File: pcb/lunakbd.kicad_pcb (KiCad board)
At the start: 2 copper layers, 134.4 x 112.7 mm, 64 parts, among them J1 TRRS-PJ-320D, J2 Battery_Socket, J3 Conn_Display, SW1 Switch, SW10 Switch, SW11 Switch, SW12 Switch, SW13 Switch, SW14 Switch, SW15 Switch, SW16 Switch, SW17 Switch, SW18 Switch, SW19 Switch, SW2 Switch, SW20 Switch, SW21 Switch, SW22 Switch, SW23 Switch, SW24 Switch, SW25 Switch, SW26 Switch, SW27 Switch, SW28 Switch, SW29 RotaryEncoder_SW, SW3 Switch, SW30 Reset_Button, SW31 Battery_Switch, SW4 Switch, SW5 Switch, SW6 Switch, SW7 Switch, SW8 Switch, SW9 Switch, U1 ProMicro

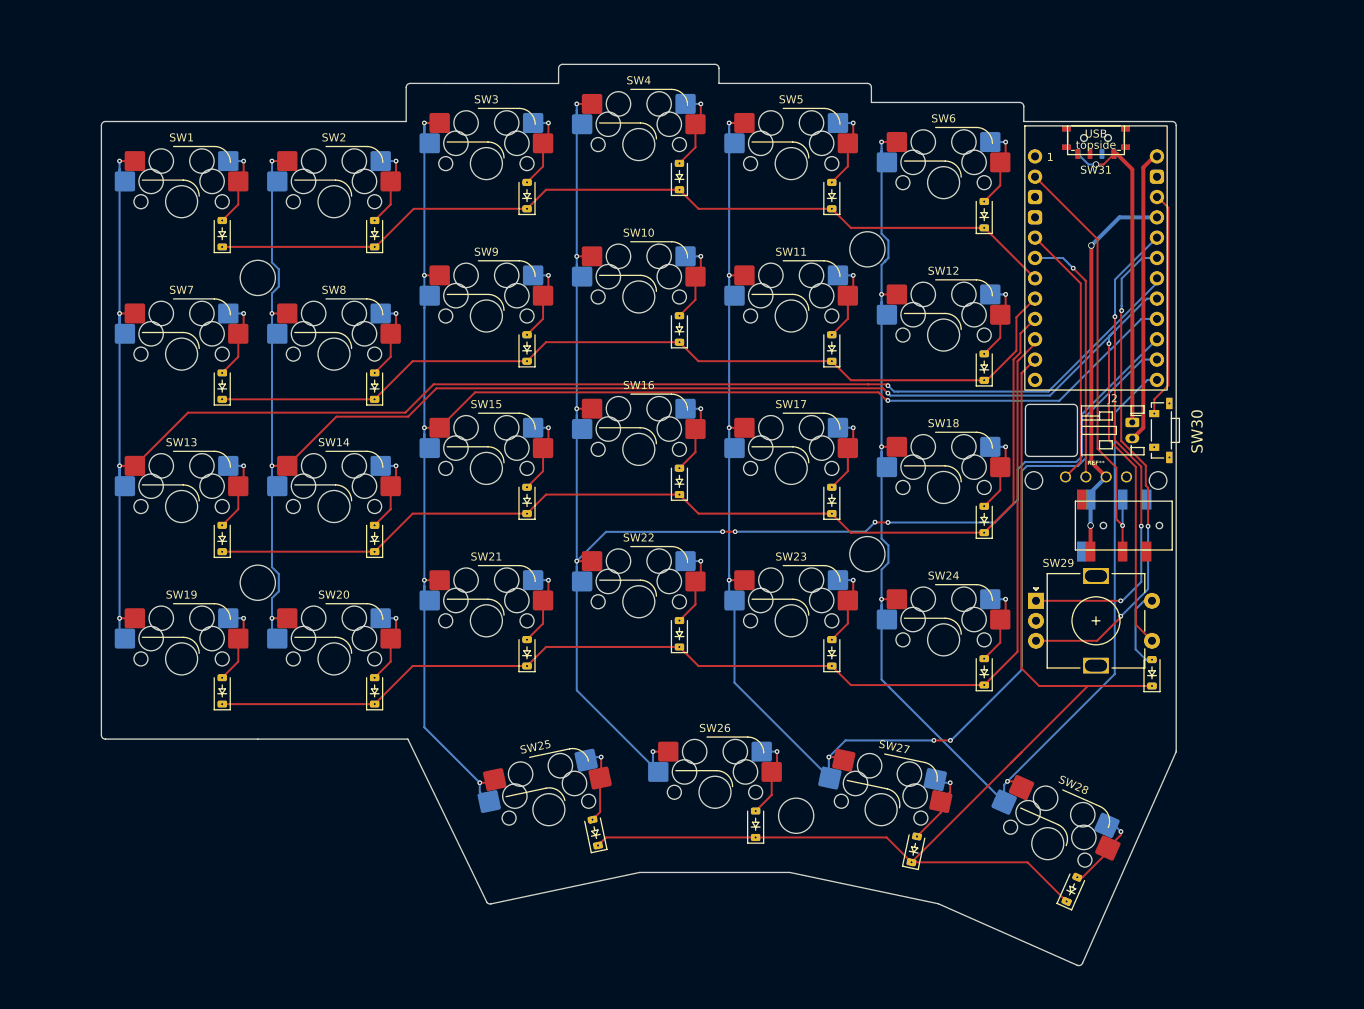
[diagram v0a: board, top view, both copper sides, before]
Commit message: feat: create ground zone
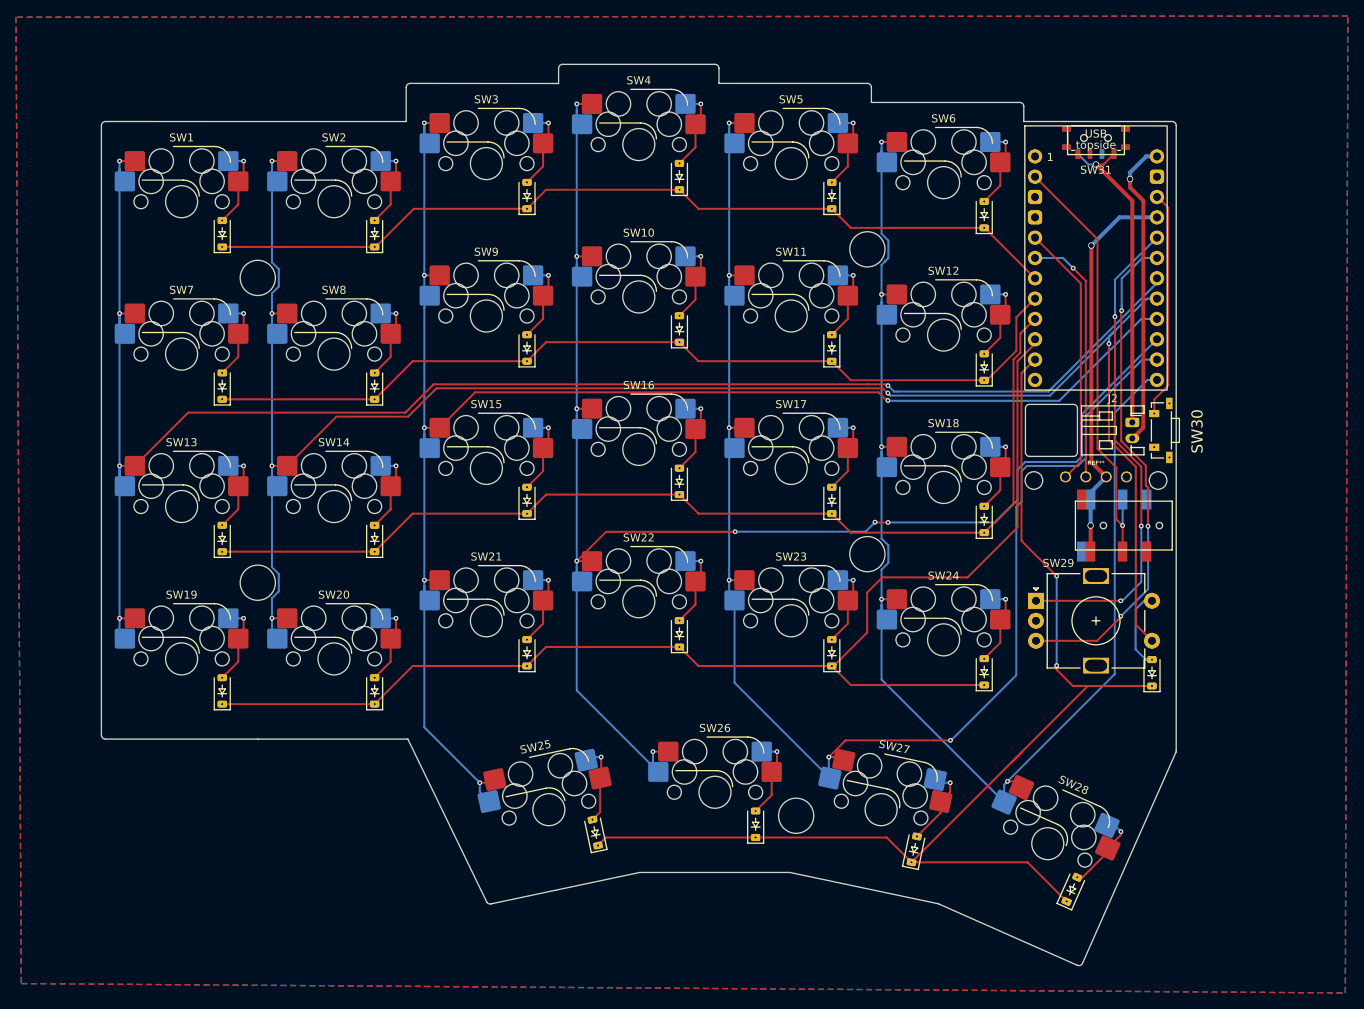
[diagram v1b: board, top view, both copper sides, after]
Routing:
- net row-3: track 146.2 -> 158.2 mm
- net row-4: track 152.8 -> 150.3 mm, vias 0 -> 2
- net B+: track 37.0 -> 39.3 mm, vias 0 -> 1
- net B-: track 40.3 -> 39.7 mm
- net col-3: vias 9 -> 8
- net col-4: vias 7 -> 6
- added copper zone on B.Cu, net GND
- added copper zone on F.Cu, net GND

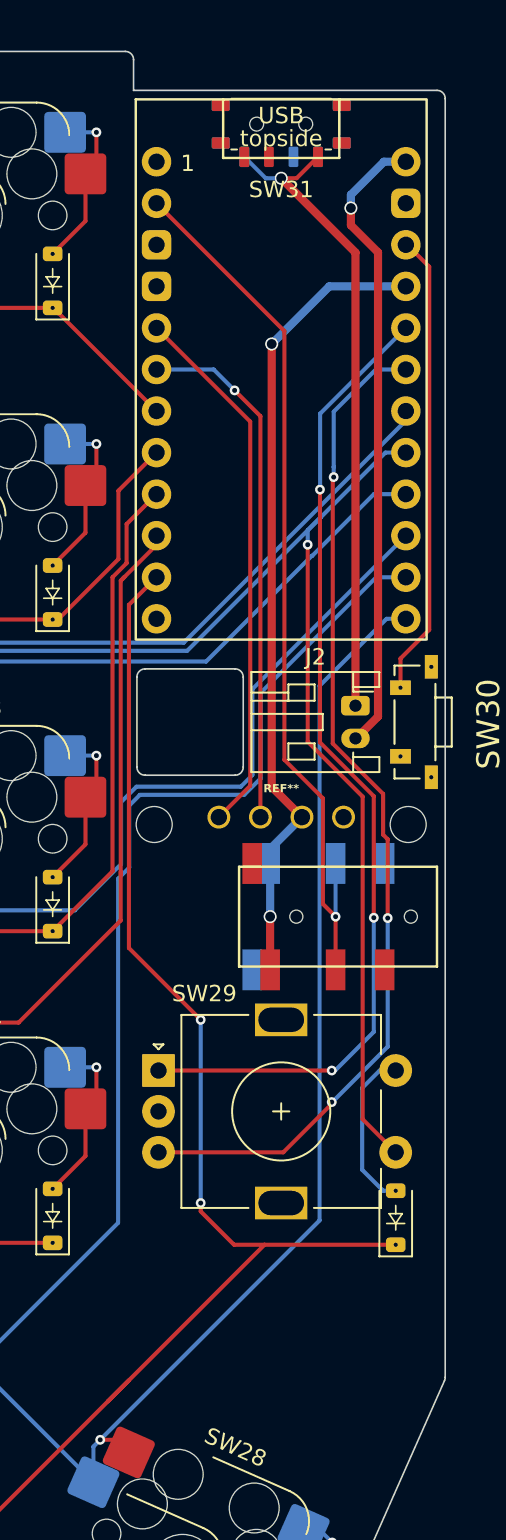
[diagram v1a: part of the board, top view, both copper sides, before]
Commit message: fix: connection for oled inversion
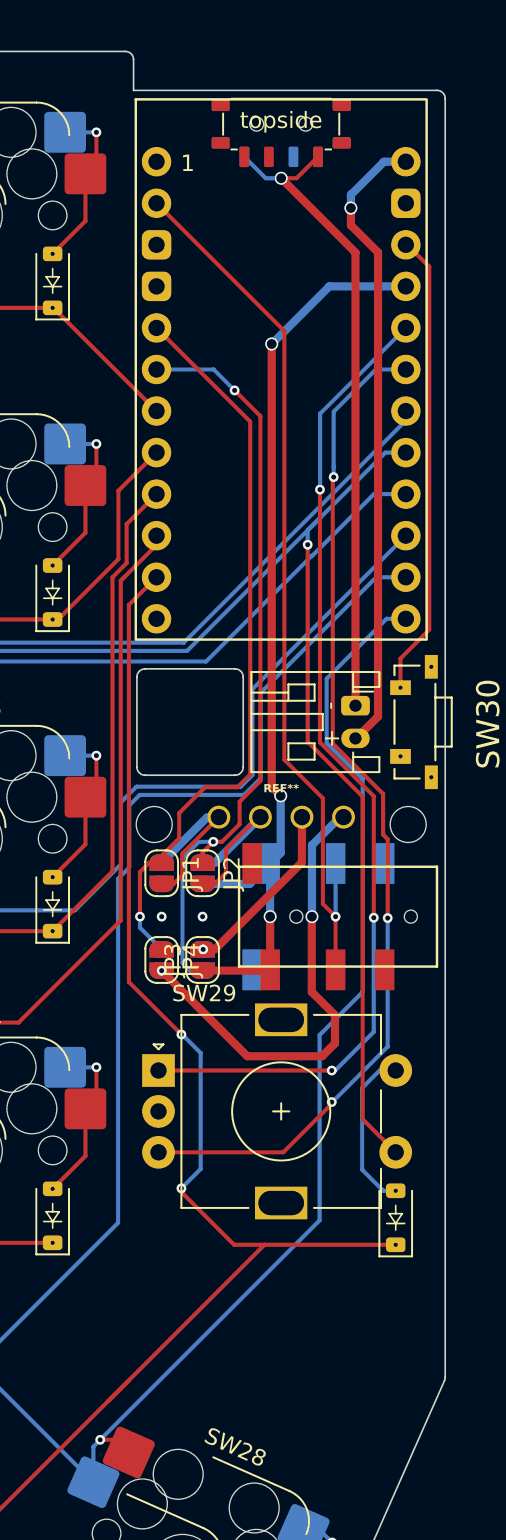
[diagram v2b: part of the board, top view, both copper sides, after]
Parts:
- added JP1: Jumper, Jumper:SolderJumper-2_P1.3mm_Open_RoundedPad1.0x1.5mm, F.Cu at (183.2, 90.2)
- added JP2: Jumper, Jumper:SolderJumper-2_P1.3mm_Open_RoundedPad1.0x1.5mm, F.Cu at (185.7, 90.2)
- added JP3: Jumper, Jumper:SolderJumper-2_P1.3mm_Open_RoundedPad1.0x1.5mm, F.Cu at (185.7, 95.5)
- added JP4: Jumper, Jumper:SolderJumper-2_P1.3mm_Open_RoundedPad1.0x1.5mm, F.Cu at (183.2, 95.5)
- added JP5: Jumper, Jumper:SolderJumper-2_P1.3mm_Open_RoundedPad1.0x1.5mm, B.Cu at (183.2, 90.2)
- added JP6: Jumper, Jumper:SolderJumper-2_P1.3mm_Open_RoundedPad1.0x1.5mm, B.Cu at (185.7, 90.2)
- added JP7: Jumper, Jumper:SolderJumper-2_P1.3mm_Open_RoundedPad1.0x1.5mm, B.Cu at (185.7, 95.5)
- added JP8: Jumper, Jumper:SolderJumper-2_P1.3mm_Open_RoundedPad1.0x1.5mm, B.Cu at (183.2, 95.5)
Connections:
- J3 pad 1: sda -> Net-(J3-Pin_1)
- J3 pad 2: sdl -> Net-(J3-Pin_2)
- J3 pad 3: VCC -> Net-(J3-Pin_3)
- J3 pad 4: GND -> Net-(J3-Pin_4)
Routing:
- net Net-(J3-Pin_4): track 0.00 -> 28.4 mm, vias 0 -> 2
- net sdl: track 32.0 -> 46.7 mm, vias 1 -> 2
- net sda: track 33.1 -> 45.3 mm, vias 0 -> 1
- net Net-(J3-Pin_2): track 0.00 -> 11.4 mm
- net Net-(J3-Pin_3): track 0.00 -> 11.0 mm, vias 0 -> 1
- net Net-(J3-Pin_1): track 0.00 -> 10.6 mm
- net VCC: track 49.5 -> 58.1 mm, vias 2 -> 3
- net col-5: track 169.4 -> 171.2 mm
- net row-4: track 150.3 -> 151.3 mm
- net GND: vias 0 -> 2
